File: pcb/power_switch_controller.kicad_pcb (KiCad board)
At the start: 2 copper layers, 118.1 x 54.6 mm, 64 parts, among them P1 PWR_JACK_2.5x5.5, P2 HEADER_01X03, P3 BNC_DOUBLE_RA, P4 HEADER_02X08_SMD, P5 HEADER_02X08_SMD, P6 HEADER_02X08_SMD, P7 HEADER_02X08_SMD, SW1 SPST_SERIES_M, SW2 KT_SWITCH, U1 MAX6817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

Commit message: JaneliaSciComp -> janelia-modular-devices.
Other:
- board text added: "https://github.com/janelia-modular-devices/modular-devices"
- board text removed: "https://github.com/JaneliaSciComp/modular-devices"
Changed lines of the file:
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@@
     (effects (font (size 1.016 1.016) (thickness 0.254)))
   )
-  (gr_text https://github.com/JaneliaSciComp/modular-devices (at 189.23 102.87 90) (layer F.SilkS)
+  (gr_text https://github.com/janelia-modular-devices/modular-devices (at 189.23 102.87 90) (layer F.SilkS)
     (effects (font (size 0.762 0.762) (thickness 0.1905)))
   )

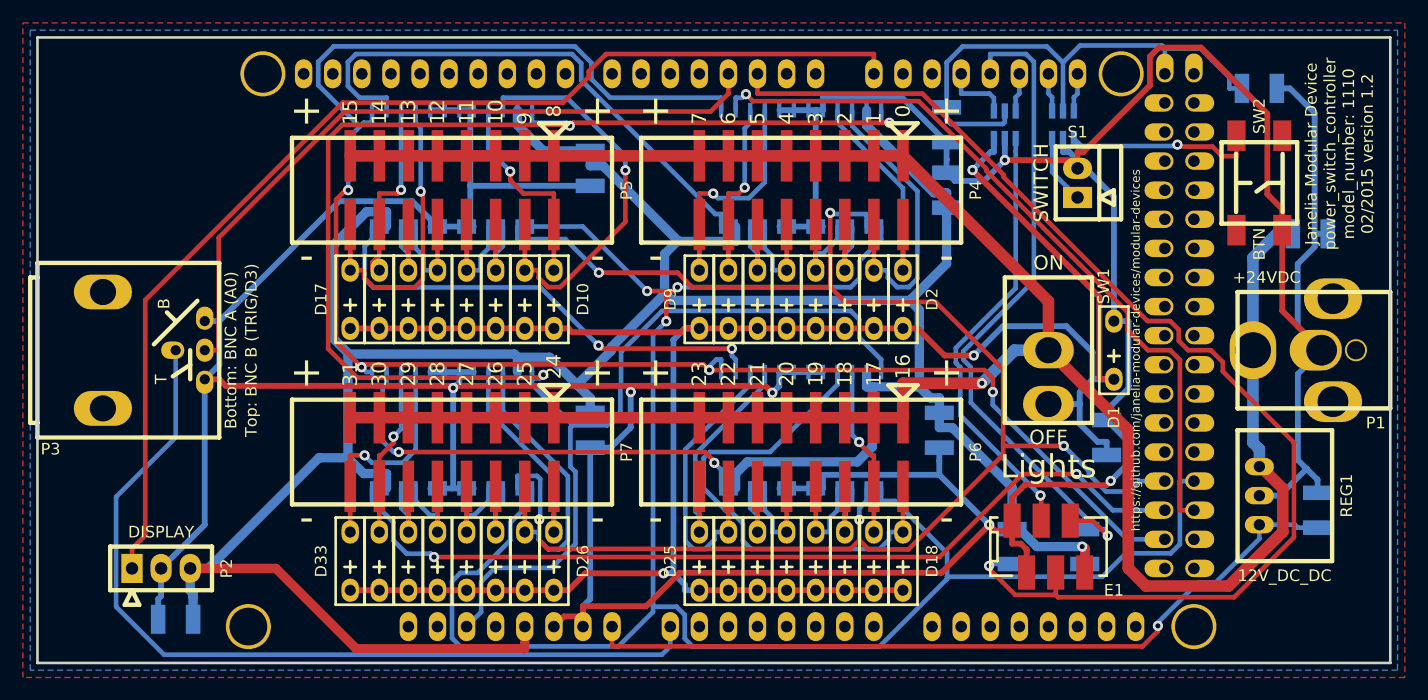
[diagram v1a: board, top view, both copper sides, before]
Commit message: SPST switch -> DPST switch.
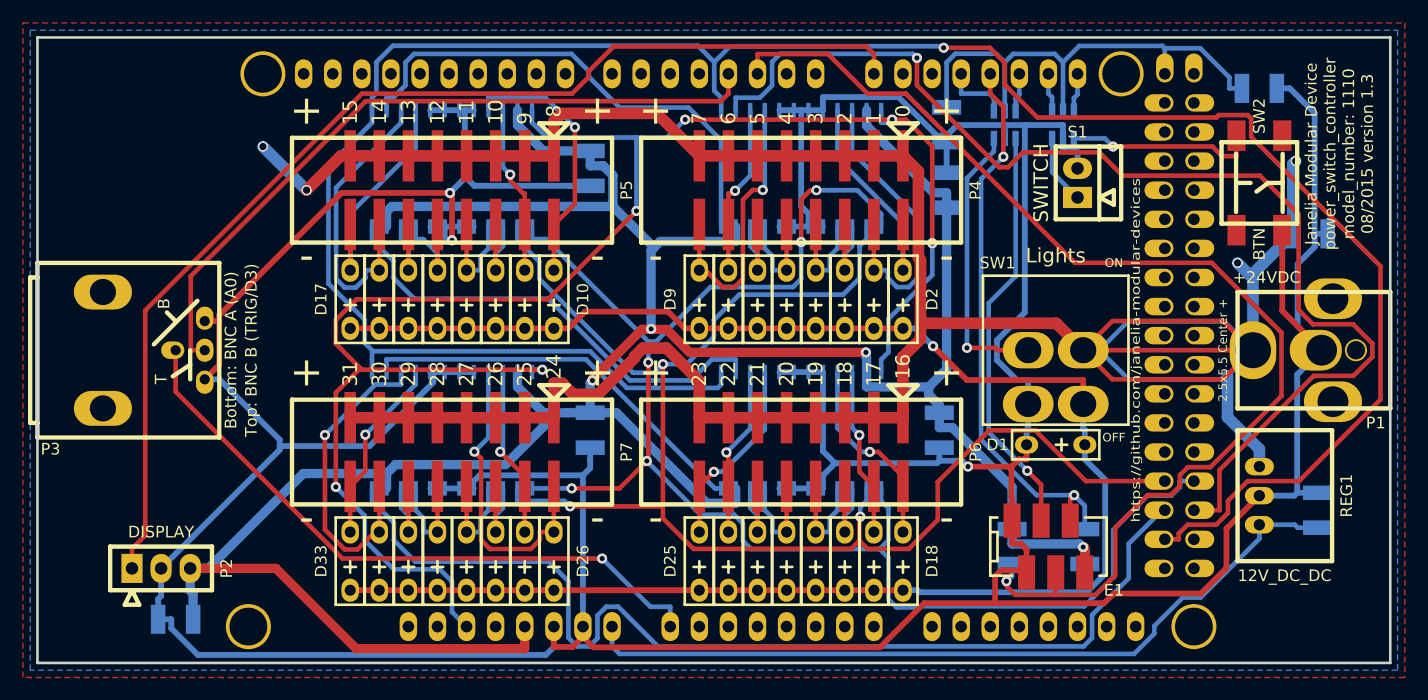
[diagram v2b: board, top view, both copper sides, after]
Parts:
- removed R3: 5.11k, power_switch_controller:SM1210
- SW1: value SPST_SERIES_M -> DPST_SERIES_M; footprint power_switch_controller:SPST_SERIES_M -> power_switch_controller:DPST_SERIES_M
- moved D1 9.69 mm to (182.2, 111.1), turned to 270 degrees
- moved SW1 0.63 mm to (182.2, 102.9)
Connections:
- net /D_LED_PWR renamed /D_LIGHTS
- U1 pad 3: /LED_PWR -> /LIGHTS
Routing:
- net VAA: track 203.1 -> 270.6 mm, vias 1 -> 4
- net /SCK: track 153.6 -> 203.9 mm, vias 4 -> 1
- net /MOSI: track 65.0 -> 101.7 mm
- net /CS: track 171.1 -> 137.5 mm, vias 3 -> 5
- net /LED_PWR: track 184.2 -> 151.6 mm, vias 3 -> 1
- net /OUT16: track 43.6 -> 17.2 mm, vias 0 -> 1
- net /LIGHTS: track 0.00 -> 24.7 mm, vias 0 -> 1
- net /OUT9: track 35.8 -> 14.8 mm
- net /BNC_A: track 76.7 -> 56.3 mm, vias 0 -> 1
- net /MISO: track 77.6 -> 91.2 mm, vias 2 -> 0
- net /OUT30: track 14.8 -> 28.1 mm
- net /RST: track 164.0 -> 151.1 mm, vias 3 -> 6
- net /OUT22: track 26.1 -> 14.9 mm, vias 0 -> 1
- net /OUT25: track 26.2 -> 15.0 mm, vias 0 -> 1
- net /ENC_A: track 59.8 -> 49.1 mm, vias 1 -> 2
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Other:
- board text added: "2.5x5.5 Center +"
- board text added: "Janelia Modular Device power_switch_controller model_number: 1110 08/2015 version 1.3"
- board text added: "https://github.com/janelia-modular-devices"
- board text removed: "Janelia Modular Device power_switch_controller model_number: 1110 02/2015 version 1.2"
- board text removed: "https://github.com/janelia-modular-devices/modular-devices"
